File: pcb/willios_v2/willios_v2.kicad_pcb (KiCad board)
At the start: 4 copper layers, 55 parts, among them J1 Screw_Terminal_01x02, J10 Conn_01x01_Female, J11 Conn_01x01_Female, J12 Conn_01x01_Female, J2 USB_B_Micro, J3 SWD, J4 Conn_01x04_Female, J5 Conn_01x04_Female, J6 Conn_01x06_Female, J7 Conn_01x01_Female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

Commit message: Established layout and cut
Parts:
- moved J4 44.4 mm to (129.8, 154.5), turned to 270 degrees
- moved C5 34.7 mm to (105.5, 131.8), turned to 180 degrees
- moved J8 23.8 mm to (92.5, 134.0)
- moved J6 22.3 mm to (104.8, 154.5)
- moved R7 17.4 mm to (95.0, 150.8), turned to 270 degrees
- moved J5 15.1 mm to (92.2, 154.5)
- moved H3 15.1 mm to (86.0, 153.8)
- moved H4 12.9 mm to (138.2, 153.8)
- moved R6 12.4 mm to (131.8, 128.2)
- moved R8 11.4 mm to (97.2, 150.8), turned to 270 degrees
- moved D3 11.3 mm to (131.8, 126.5)
- moved H1 10.9 mm to (86.0, 119.2)
- moved J11 10.7 mm to (86.0, 130.2)
- moved J10 10.2 mm to (86.0, 139.2)
- moved H2 9.91 mm to (138.2, 119.2)
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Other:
- board outline added: 61.2 x 43.5 mm

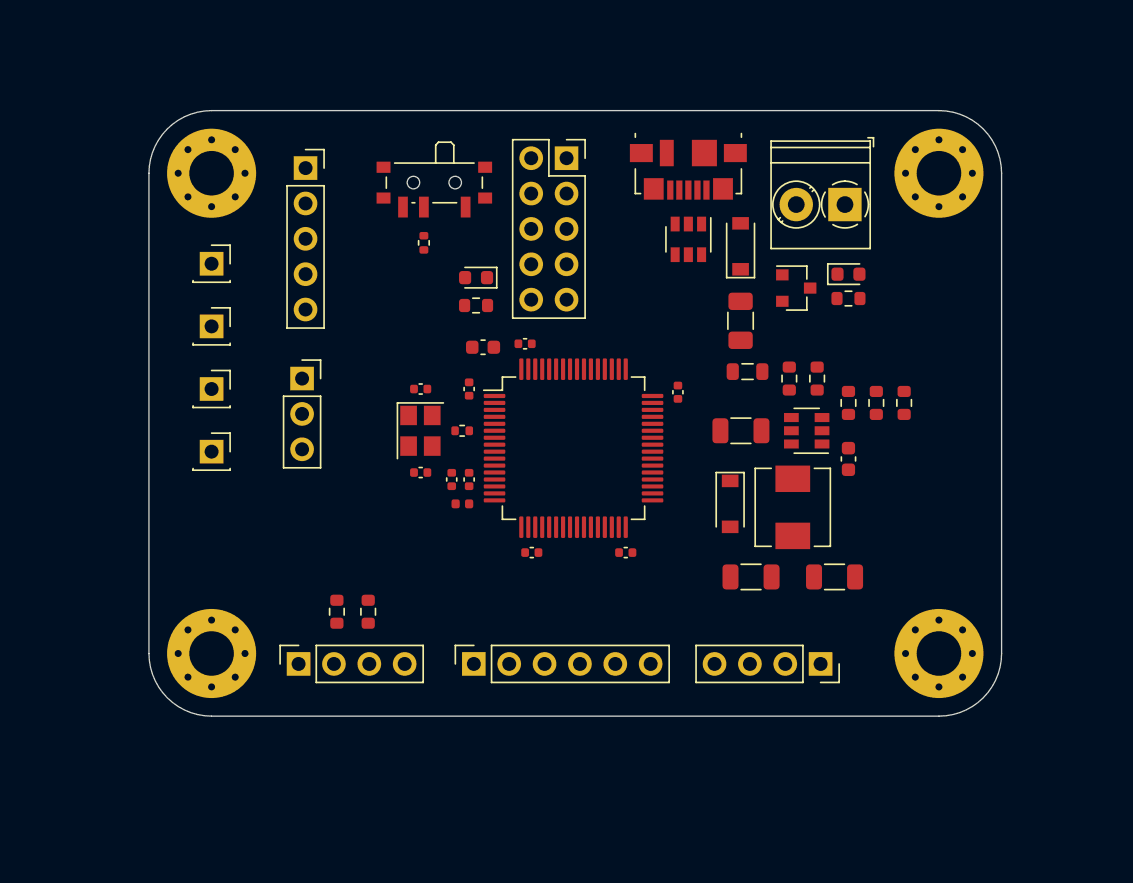
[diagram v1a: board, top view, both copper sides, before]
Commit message: Routing pre-oscillator
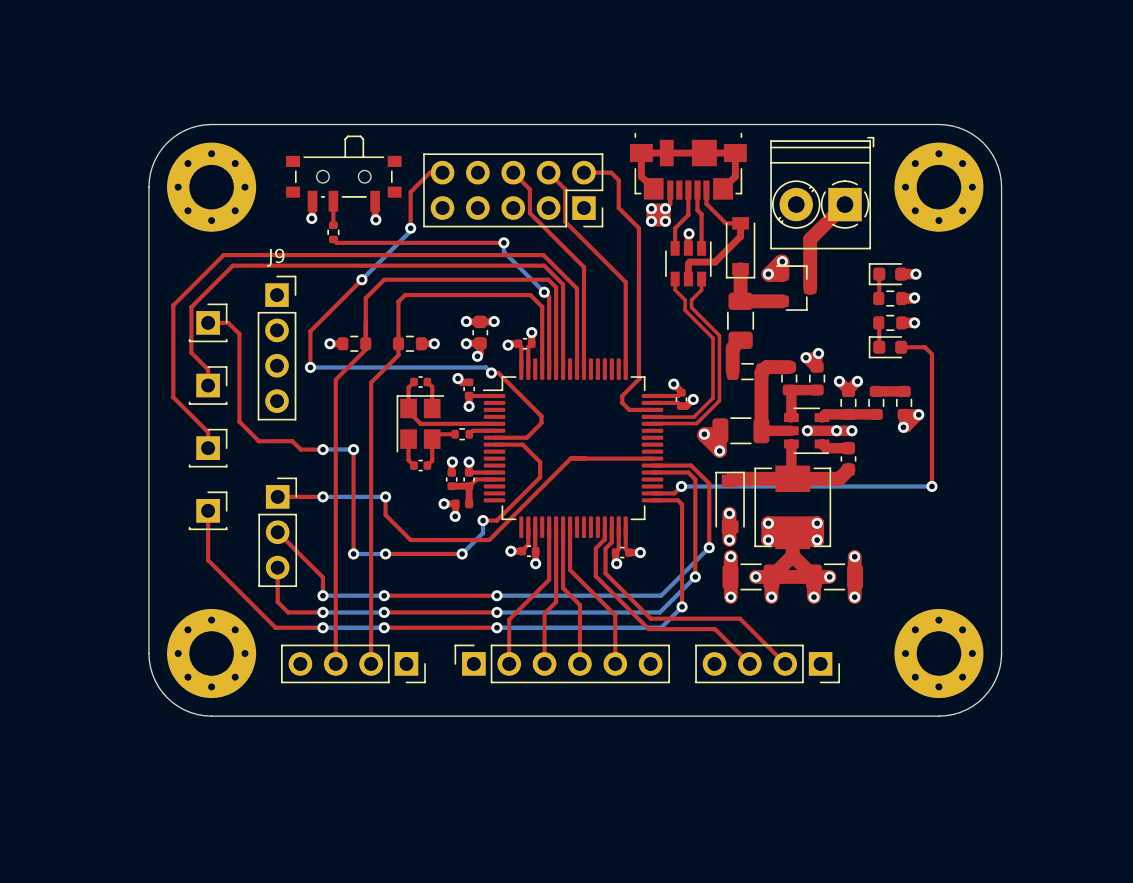
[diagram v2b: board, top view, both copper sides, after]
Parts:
- J9: value Conn_01x05_Female -> Conn_01x04_Female; footprint Connector_PinSocket_2.54mm:PinSocket_1x05_P2.54mm_Vertical -> Connector_PinSocket_2.54mm:PinSocket_1x04_P2.54mm_Vertical
- moved D4 30.2 mm to (134.8, 131.8), turned to 0 degrees
- moved R11 29.8 mm to (134.8, 130.0), turned to 0 degrees
- moved R7 20.0 mm to (100.2, 131.5), turned to 180 degrees
- moved R8 19.3 mm to (96.2, 131.5), turned to 0 degrees
- moved J9 9.35 mm to (90.7, 128.0)
- moved J11 8.75 mm to (85.8, 139.0)
- moved J8 8.68 mm to (90.8, 142.5)
- moved J5 7.75 mm to (100.0, 154.5), turned to 270 degrees
- moved R9 6.54 mm to (94.8, 123.5)
- moved SW1 6.51 mm to (95.5, 119.8)
- moved J10 4.26 mm to (85.8, 143.5)
- moved J7 4.26 mm to (85.8, 130.0)
- moved J3 3.79 mm to (112.8, 121.8), turned to 270 degrees
- moved D3 3.00 mm to (134.8, 126.5)
- moved R6 3.00 mm to (134.8, 128.2)
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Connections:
- J9 pad 3: +3.3VA -> GND
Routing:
- net GND: track 0.00 -> 59.5 mm, vias 0 -> 34
- net +3V3: track 0.00 -> 55.0 mm, vias 0 -> 23
- net PB12_GPIO: track 0.00 -> 49.8 mm, vias 0 -> 4
- net I2C1_SDA: track 0.00 -> 49.2 mm
- net TIM3_CH1: track 0.00 -> 48.6 mm
- net ADC1_IN1: track 0.00 -> 46.5 mm, vias 0 -> 6
- net PC7_GPIO: track 0.00 -> 44.3 mm, vias 0 -> 4
- net PC6_GPIO: track 0.00 -> 44.1 mm, vias 0 -> 4
- net I2C1_SCL: track 0.00 -> 42.2 mm
- net NRST: track 0.00 -> 40.8 mm, vias 0 -> 4
- net TIM4_CH1: track 0.00 -> 40.7 mm
- net PC8_GPIO: track 0.00 -> 32.4 mm, vias 0 -> 2
- net LED_STATUS: track 0.00 -> 32.2 mm, vias 0 -> 2
- net BOOT0: track 0.00 -> 22.8 mm, vias 0 -> 2
- net SWDIO: track 0.00 -> 22.2 mm
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- added copper zone on In2.Cu, net +3V3
- added copper zone on In1.Cu, net GND
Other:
- board size 61.2 x 43.5 mm -> 61.2 x 42.5 mm

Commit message: Completed layout willios v2
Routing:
- net NRST: track 40.8 -> 33.6 mm, vias 4 -> 2
- net GND: track 59.5 -> 62.7 mm, vias 34 -> 36
- added copper zone on B.Cu, net GND
- added copper zone on F.Cu, net GND
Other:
- outline, holes or cut-outs redrawn
- board text added: "+"
- board text added: "3 GPIO"
- board text added: "ADC"
- board text added: "BOOT"
- board text added: "GPIO"
- board text added: "I2C"
- board text added: "JLCJLCJLCJLC"
- board text added: "POWER RAIL"
- board text added: "PWM0"
- board text added: "PWM1"
- board text added: "RUN"
- board text added: "SPI"
- board text added: "SWD"
- board text added: "UART"
- board text added: "willios v2"
